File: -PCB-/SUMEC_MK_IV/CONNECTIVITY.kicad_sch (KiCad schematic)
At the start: 0 parts

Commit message: DC-DC conv added
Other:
- company: (none) -> SPS NA PROSEKU
- title: (none) -> SUMEC_MK_IV
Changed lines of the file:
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@@
 	(generator_version "8.0")
 	(paper "A4")
+	(title_block
+		(title "SUMEC_MK_IV")
+		(date "2024-07-01")
+		(company "SPS NA PROSEKU")
+		(comment 1 "SAVVA POPOV")
+	)
 )

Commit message: added stab. VBUS, USB connection
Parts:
- added C?: 100nF, Capacitor_SMD:C_0805_2012Metric_Pad1.18x1.45mm_HandSolder, symbol Device:C
- added D?: D_Schottky, Diode_SMD:D_1206_3216Metric_Pad1.42x1.75mm_HandSolder, symbol Device:D_Schottky
- added J?: TYPE-C-31-M-12, sumec-smdV2_library:USB_Type_C, symbol sumec_library:TYPE-C-31-M-12
- added R? (x2): 15R, Resistor_SMD:R_0805_2012Metric_Pad1.20x1.40mm_HandSolder, symbol Device:R
- added R?: 0R, Resistor_SMD:R_1206_3216Metric_Pad1.30x1.75mm_HandSolder, symbol Device:R
- added U?: USBLC6-2SC6, Package_TO_SOT_SMD:TSOT-23-6_HandSoldering, symbol sumec_library:USBLC6-2SC6
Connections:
- new net: R?.2, U?.1
- new net: R?.2, U?.3
- new net: D?.2 (A), J?.A4_B9 (VBUS), J?.B4_A9 (VBUS)
- new net: J?.S1 (SHIELD), J?.S2 (SHIELD), J?.S3 (SHIELD), J?.S4 (SHIELD), R?.1
- new net D+: U?.6
- new net D+ IN: J?.A6 (DP1), J?.B6 (DP2), R?.1
- new net D-: U?.4
- new net D- IN: J?.A7 (DN1), J?.B7 (DN2), R?.1
- new net GND: C?.2, J?.A1_B12 (GND), J?.B1_A12 (GND), R?.2, U?.2
- new net VBUS 5V: C?.1, D?.1 (K), U?.5
- no-connect marks 0 -> 4
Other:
- note added: "Data transfer USB connector connected to ESP32 using CDC method"
- note added: "ESD PROTECTION"
- note added: "GPIO USB 20 D+ (green) 19 D- (white) GND GND (black) NC +5V (red)"
- note added: "TESTED - WORKS, INSPECTED"
- note added: "USB"
- note added: "USB CONNECTOR"
- note added: "USB Type-C Connector"

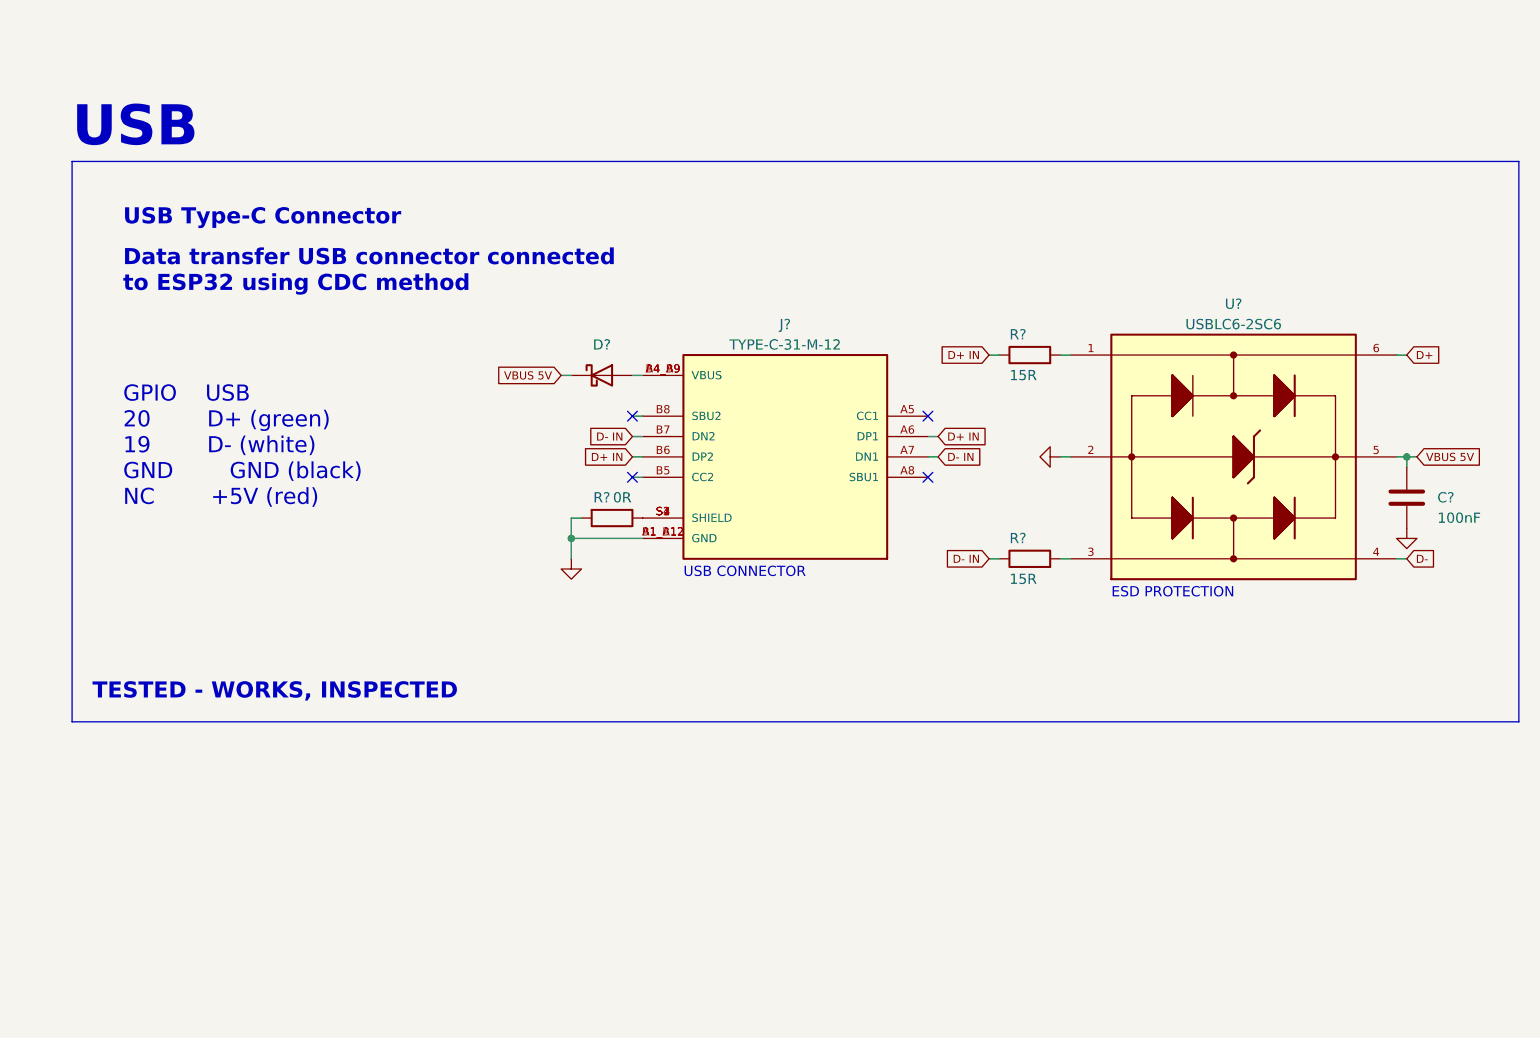
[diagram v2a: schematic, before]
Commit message: VBATT VBUS Switching
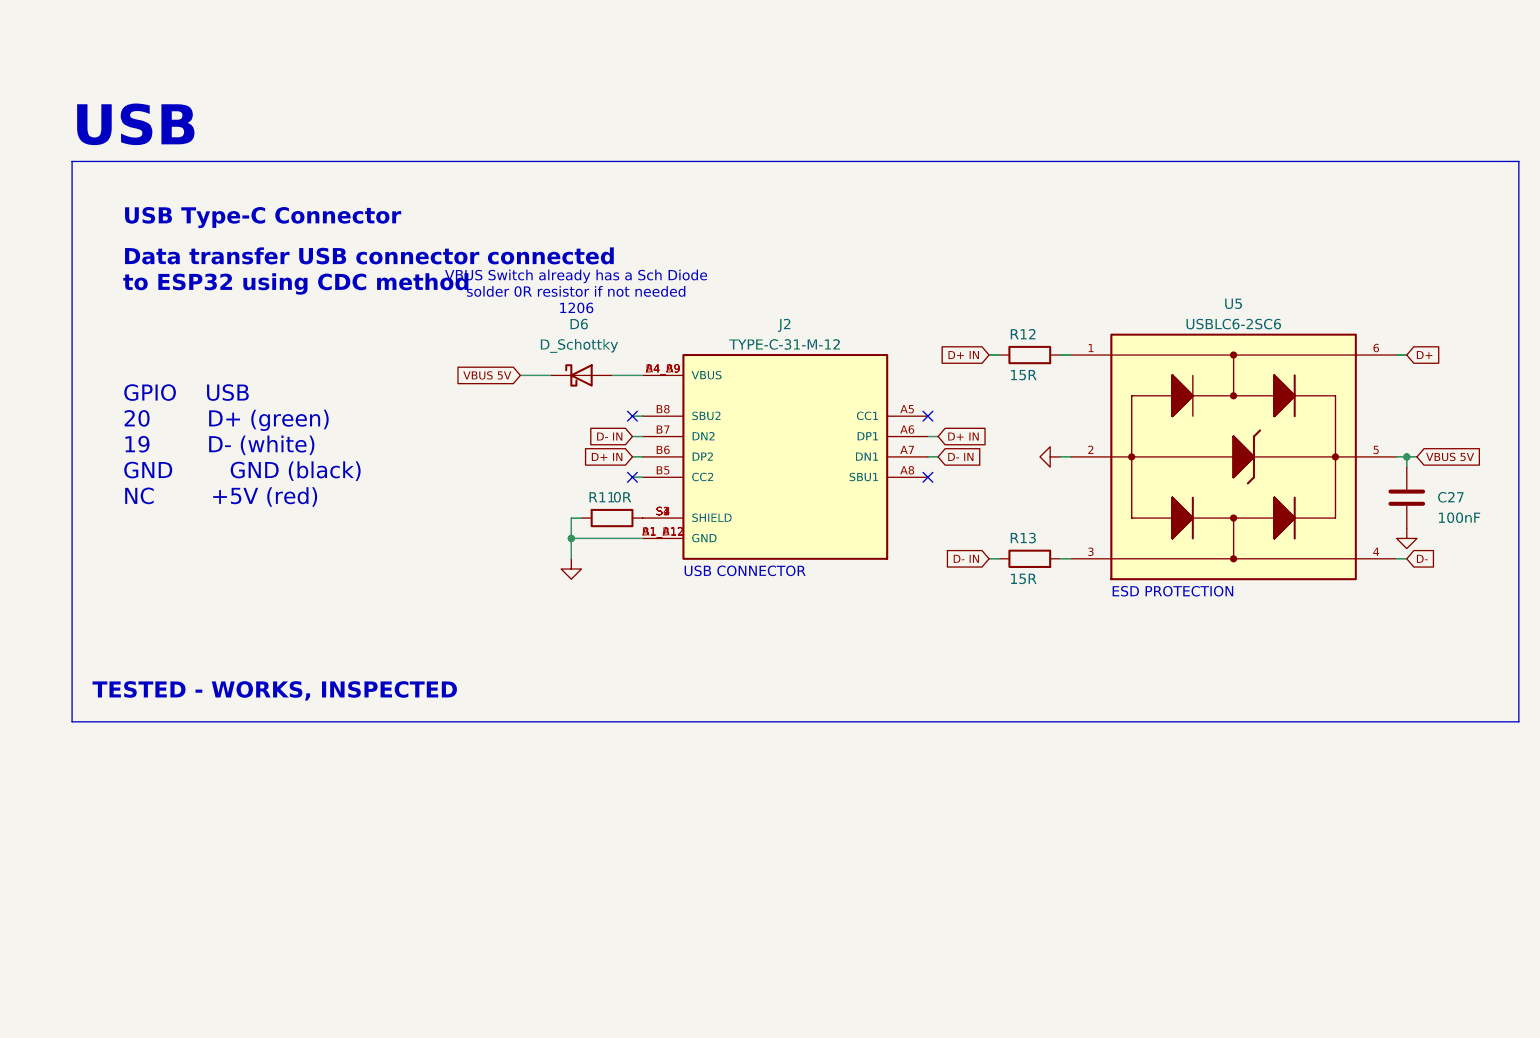
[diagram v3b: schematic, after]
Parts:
- removed D?: D_Schottky, Diode_SMD:D_1206_3216Metric_Pad1.42x1.75mm_HandSolder, symbol Device:D_Schottky
- added D6: D_Schottky, symbol Device:D_Schottky
- gave numbers to parts that had none: 6
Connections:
- net VBUS 5V: now also D6.1 (K)
- net at J2.A4_B9 (VBUS), J2.B4_A9 (VBUS): now also D6.2 (A)
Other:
- note added: "VBUS Switch already has a Sch Diode solder 0R resistor if not needed 1206"
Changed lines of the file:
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@@
 	(wire
 		(pts
-			(xy 125.73 78.74) (xy 127 78.74)
+			(xy 179.07 101.6) (xy 180.34 101.6)
 		)
 		(stroke
@@
 	(wire
 		(pts
-			(xy 179.07 101.6) (xy 180.34 101.6)
+			(xy 179.07 76.2) (xy 180.34 76.2)
 		)
 		(stroke
@@
 	(wire
 		(pts
-			(xy 179.07 76.2) (xy 180.34 76.2)
+			(xy 179.07 88.9) (xy 180.34 88.9)
 		)
 		(stroke
@@
 	(wire
 		(pts
-			(xy 179.07 88.9) (xy 180.34 88.9)
+			(xy 223.52 88.9) (xy 222.25 88.9)
 		)
 		(stroke
@@
 	(wire
 		(pts
-			(xy 223.52 88.9) (xy 222.25 88.9)
+			(xy 163.83 88.9) (xy 162.56 88.9)
 		)
 		(stroke
@@
 	(wire
 		(pts
-			(xy 163.83 88.9) (xy 162.56 88.9)
+			(xy 123.19 78.74) (xy 127 78.74)
 		)
 		(stroke
@@
 	(wire
 		(pts
-			(xy 116.84 78.74) (xy 118.11 78.74)
+			(xy 111.76 78.74) (xy 115.57 78.74)
 		)
 		(stroke
@@
 		)
 	)
+	(text "VBUS Switch already has a Sch Diode\nsolder 0R resistor if not needed\n1206"
+		(exclude_from_sim no)
+		(at 118.745 68.58 0)
+		(effects
+			(font
+				(size 1.27 1.27)
+				(color 255 0 0 1)
+			)
+		)
+	)
 	(text "GPIO	USB\n20		D+ (green)\n19		D- (white)\nGND		GND (black)\nNC		+5V (red)"
 		(exclude_from_sim no)
@@
 	(global_label "VBUS 5V"
 		(shape input)
-		(at 116.84 78.74 180)
+		(at 111.76 78.74 180)
 		(fields_autoplaced yes)
 		(effects
@@
 		)
 		(property "Intersheetrefs" "${INTERSHEET_REFS}"
-			(at 108.1236 78.74 0)
+			(at 103.0436 78.74 0)
 			(effects
 				(font
@@
 		(dnp no)
 		(fields_autoplaced yes)
-		(property "Reference" "U?"
+		(property "Reference" "U5"
 			(at 200.66 69.85 0)
 			(effects
@@
 			(project "SUMEC_MK_IV"
 				(path "/900bd7ac-cdf9-4a2f-8b1f-2c21e3760046/ce2ae977-07a3-41c1-b3e1-68b5a1d5517b"
-					(reference "U?")
+					(reference "U5")
+					(unit 1)
+				)
+			)
+		)
+	)
+	(symbol
+		(lib_id "Device:D_Schottky")
+		(at 119.38 78.74 0)
+		(unit 1)
+		(exclude_from_sim no)
+		(in_bom yes)
+		(on_board yes)
+		(dnp no)
+		(fields_autoplaced yes)
+		(property "Reference" "D6"
+			(at 119.0625 72.39 0)
+			(effects
+				(font
+					(size 1.27 1.27)
+				)
+			)
+		)
+		(property "Value" "D_Schottky"
+			(at 119.0625 74.93 0)
+			(effects
+				(font
+					(size 1.27 1.27)
+				)
+			)
+		)
+		(property "Footprint" ""
+			(at 119.38 78.74 0)
+			(effects
+				(font
+					(size 1.27 1.27)
+				)
+				(hide yes)
+			)
+		)
+		(property "Datasheet" "~"
+			(at 119.38 78.74 0)
+			(effects
+				(font
+					(size 1.27 1.27)
+				)
+				(hide yes)
+			)
+		)
+		(property "Description" "Schottky diode"
+			(at 119.38 78.74 0)
+			(effects
+				(font
+					(size 1.27 1.27)
+				)
+				(hide yes)
+			)
+		)
+		(pin "2"
+		)
+		(pin "1"
+		)
+		(instances
+			(project "SUMEC_MK_IV"
+				(path "/900bd7ac-cdf9-4a2f-8b1f-2c21e3760046/ce2ae977-07a3-41c1-b3e1-68b5a1d5517b"
+					(reference "D6")
 					(unit 1)
 				)
@@
 		(on_board yes)
 		(dnp no)
-		(property "Reference" "R?"
+		(property "Reference" "R13"
 			(at 172.72 99.06 90)
 			(effects
@@
 			(project "SUMEC_MK_IV"
 				(path "/900bd7ac-cdf9-4a2f-8b1f-2c21e3760046/ce2ae977-07a3-41c1-b3e1-68b5a1d5517b"
-					(reference "R?")
+					(reference "R13")
 					(unit 1)
 				)
@@
 		(on_board yes)
 		(dnp no)
-		(property "Reference" "R?"
+		(property "Reference" "R12"
 			(at 172.72 73.66 90)
 			(effects
@@
 			(project "SUMEC_MK_IV"
 				(path "/900bd7ac-cdf9-4a2f-8b1f-2c21e3760046/ce2ae977-07a3-41c1-b3e1-68b5a1d5517b"
-					(reference "R?")
+					(reference "R12")
 					(unit 1)
 				)
@@
 		(on_board yes)
 		(dnp no)
-		(property "Reference" "J?"
+		(property "Reference" "J2"
 			(at 144.78 72.39 0)
 			(effects
@@
 			(project "SUMEC_MK_IV"
 				(path "/900bd7ac-cdf9-4a2f-8b1f-2c21e3760046/ce2ae977-07a3-41c1-b3e1-68b5a1d5517b"
-					(reference "J?")
+					(reference "J2")
 					(unit 1)
 				)
@@
 		(on_board yes)
 		(dnp no)
-		(property "Reference" "C?"
+		(property "Reference" "C27"
 			(at 226.06 93.98 0)
 			(effects
@@
 			(project "SUMEC_MK_IV"
 				(path "/900bd7ac-cdf9-4a2f-8b1f-2c21e3760046/ce2ae977-07a3-41c1-b3e1-68b5a1d5517b"
-					(reference "C?")
+					(reference "C27")
 					(unit 1)
 				)
@@
 		(on_board yes)
 		(dnp no)
-		(property "Reference" "R?"
+		(property "Reference" "R11"
 			(at 121.92 93.98 90)
 			(effects
@@
 			(project "SUMEC_MK_IV"
 				(path "/900bd7ac-cdf9-4a2f-8b1f-2c21e3760046/ce2ae977-07a3-41c1-b3e1-68b5a1d5517b"
-					(reference "R?")
+					(reference "R11")
 					(unit 1)
 				)
@@
 					(unit 1)
 				)
-			)
-		)
-	)
-	(symbol
-		(lib_id "Device:D_Schottky")
-		(at 121.92 78.74 0)
-		(unit 1)
-		(exclude_from_sim no)
-		(in_bom yes)
-		(on_board yes)
-		(dnp no)
-		(property "Reference" "D?"
-			(at 121.92 74.93 0)
-			(effects
-				(font
-					(face "Bahnschrift")
-					(size 1.27 1.27)
-				)
-			)
-		)
-		(property "Value" "D_Schottky"
-			(at 121.6025 76.2 0)
-			(effects
-				(font
-					(face "Bahnschrift")
-					(size 1.27 1.27)
-				)
-				(hide yes)
-			)
-		)
-		(property "Footprint" "Diode_SMD:D_1206_3216Metric_Pad1.42x1.75mm_HandSolder"
-			(at 121.92 78.74 0)
-			(effects
-				(font
-					(face "Bahnschrift")
-					(size 1.27 1.27)
-				)
-				(hide yes)
-			)
-		)
-		(property "Datasheet" "~"
-			(at 121.92 78.74 0)
-			(effects
-				(font
-					(face "Bahnschrift")
-					(size 1.27 1.27)
-				)
-				(hide yes)
-			)
-		)
-		(property "Description" ""
-			(at 121.92 78.74 0)
-			(effects
-				(font
-					(size 1.27 1.27)
-				)
-				(hide yes)
-			)
-		)
-		(pin "1"
-		)
-		(pin "2"
-		)
-		(instances
-			(project "SUMEC_MK_IV"
-				(path "/900bd7ac-cdf9-4a2f-8b1f-2c21e3760046/ce2ae977-07a3-41c1-b3e1-68b5a1d5517b"
-					(reference "D?")
-					(unit 1)
-				)

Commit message: MK_IV update
Power supp sheet done, mechanical sheet almost done, some changes, updates etc.
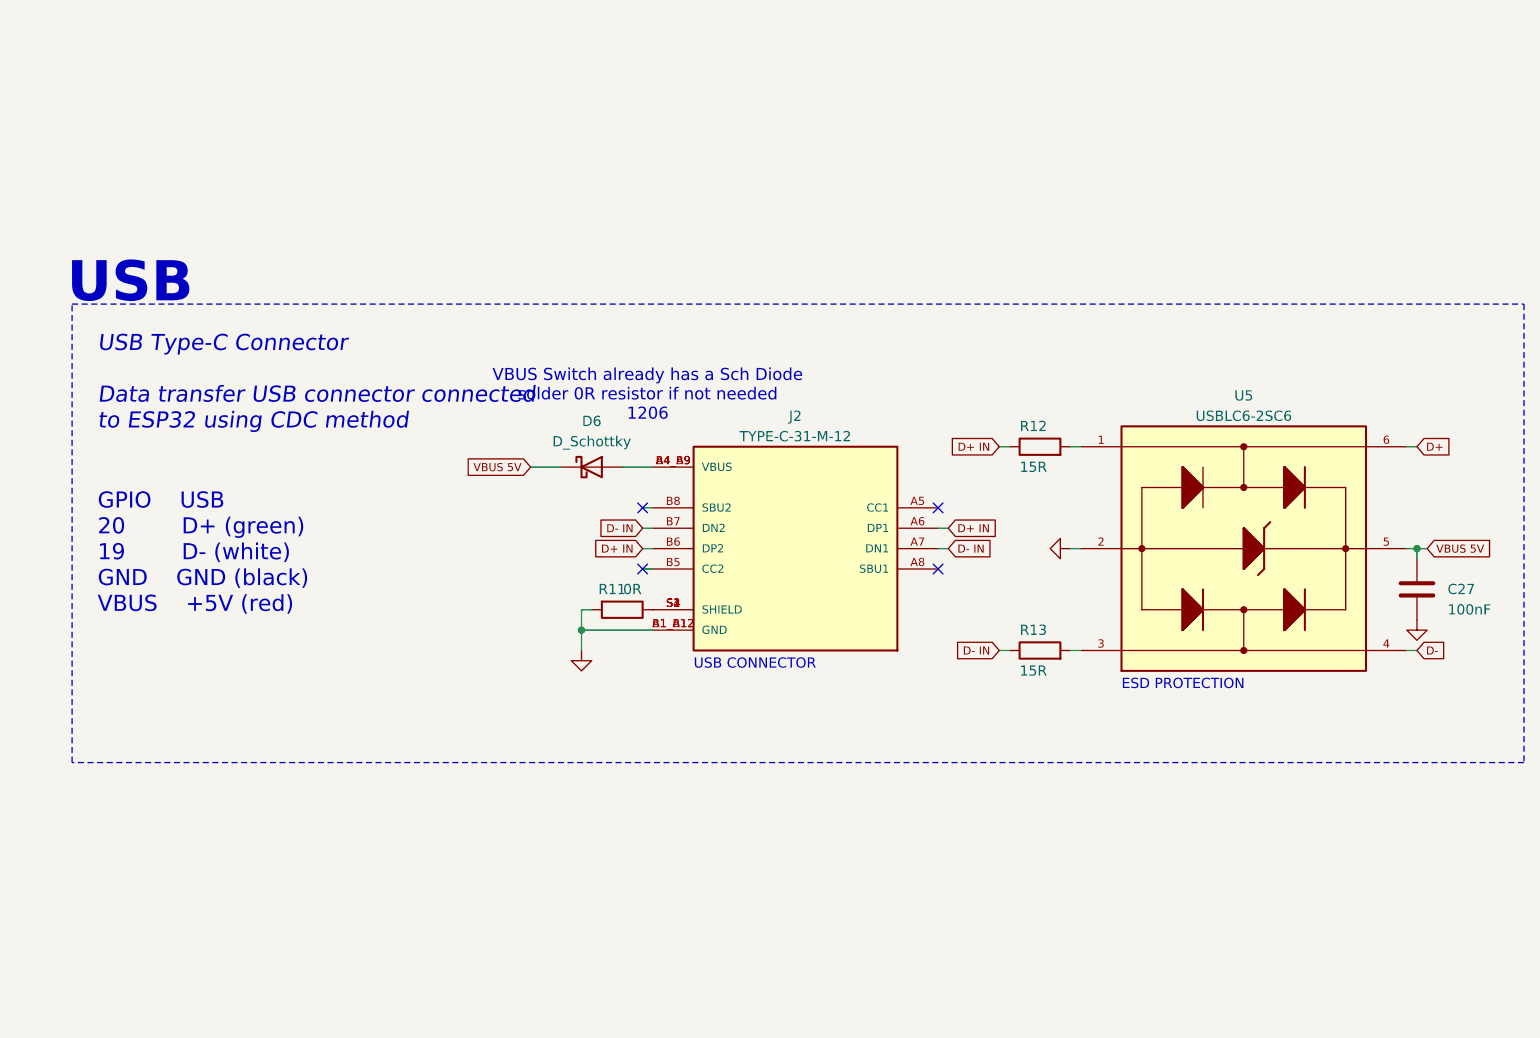
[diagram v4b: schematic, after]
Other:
- note added: "GPIO USB 20 D+ (green) 19 D- (white) GND GND (black) VBUS +5V (red)"
- note added: "USB Type-C Connector Data transfer USB connector connected to ESP32 using CDC method"
- note removed: "Data transfer USB connector connected to ESP32 using CDC method"
- note removed: "GPIO USB 20 D+ (green) 19 D- (white) GND GND (black) NC +5V (red)"
- note removed: "TESTED - WORKS, INSPECTED"
- note removed: "USB Type-C Connector"
- moved on the sheet: C27, D6, J2, R11, R12, R13, U5

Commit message: MKIV major update
Updated everything, custom symbol for ESP32, MCU sheet done, new test points added, motor control revision.

all left is to clean it up a bit
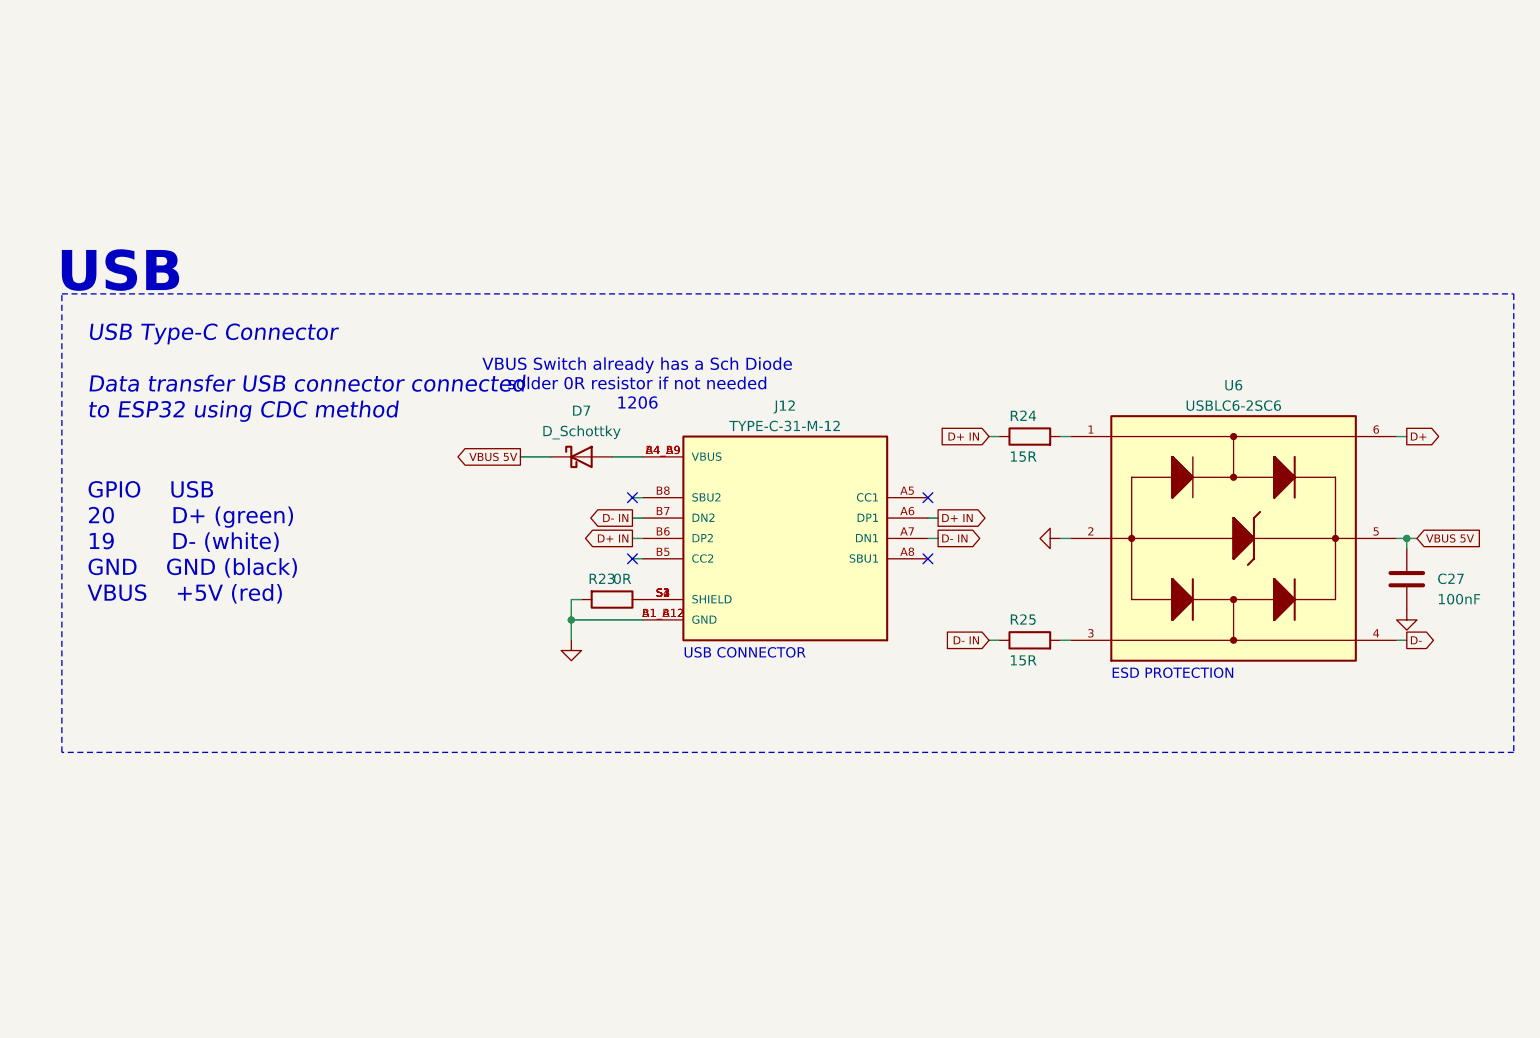
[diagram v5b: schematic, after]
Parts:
- renumbered D6 to D7, J2 to J12, R11 to R23, R12 to R24, R13 to R25, U5 to U6
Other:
- moved on the sheet: C27, D7, J12, R23, R24, R25, U6
